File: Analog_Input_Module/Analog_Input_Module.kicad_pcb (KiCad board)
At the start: 2 copper layers, 60 x 22 mm, 63 parts, among them J1 Conn_02x20_Odd_Even, U1 10K, U10 1.5K, U11 MCP6004, U12 10K, U13 10K, U14 10nF, U15 10nF, U16 MCP6004, U17 1K, U18 1K, U19 1.5K, U2 10K, U20 1.5K, U3 10nF, U4 10nF, U5 MCP6004, U6 MCP6004, U7 1K, U8 1K, U9 1.5K

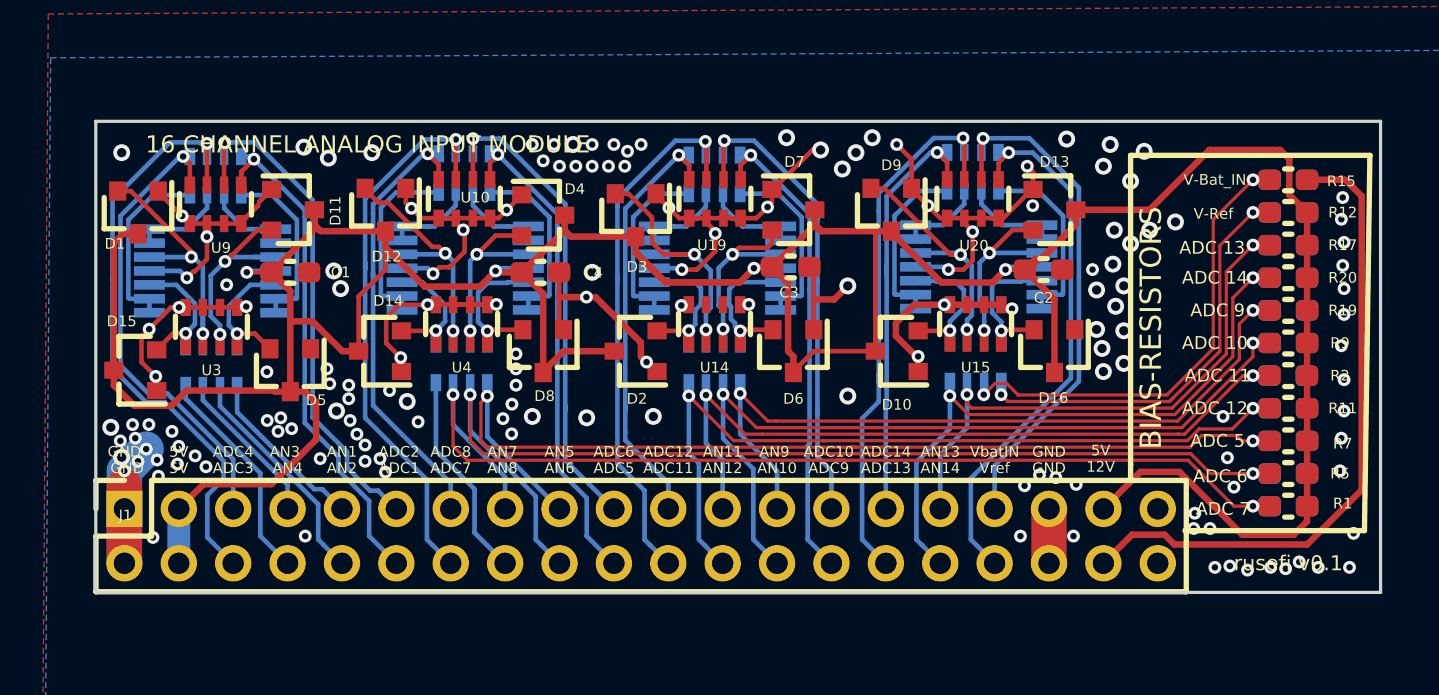
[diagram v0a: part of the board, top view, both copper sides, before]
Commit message: Corrected diode symbols and cleaned sym-lib-table
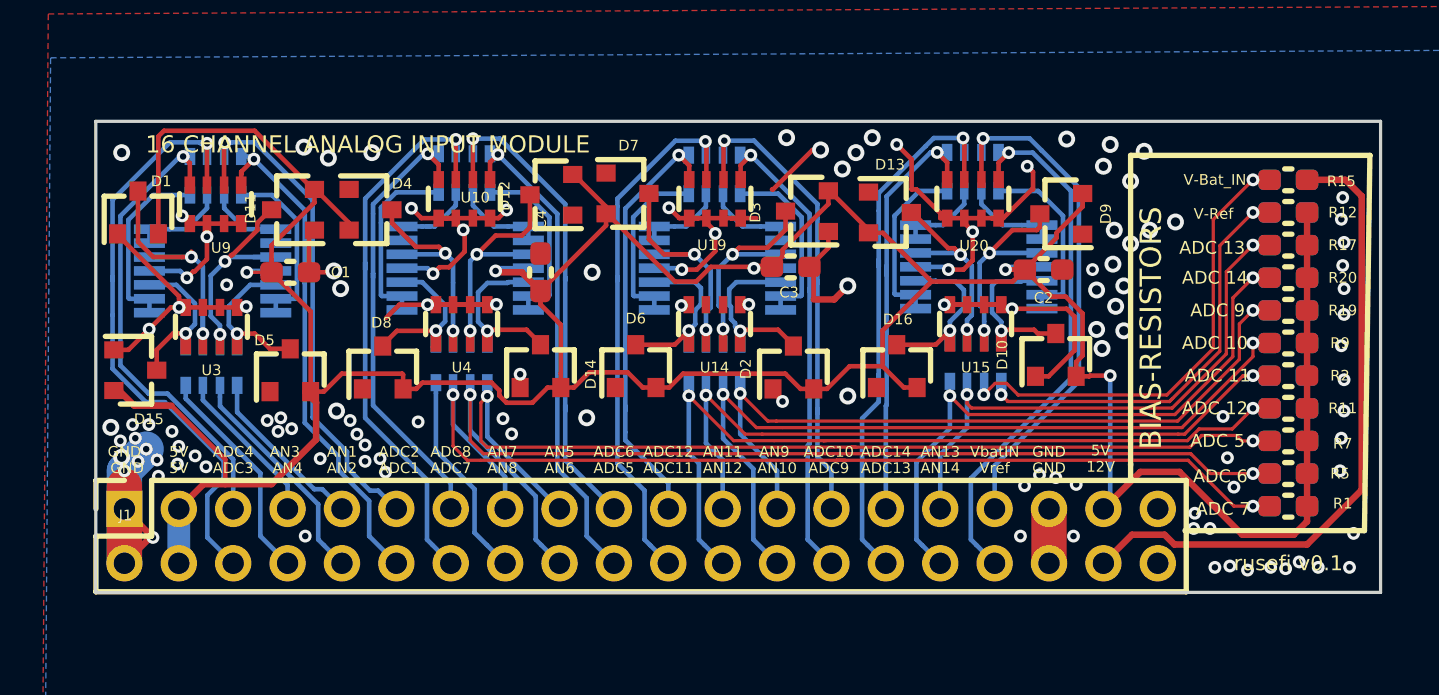
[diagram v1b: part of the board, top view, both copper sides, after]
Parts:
- moved D4 8.07 mm to (32.8, 24.1)
- moved D3 8.00 mm to (53.2, 24.2), turned to 180 degrees
- moved D9 7.94 mm to (65.1, 24.3), turned to 180 degrees
- moved D7 7.78 mm to (44.8, 23.4)
- moved D12 7.78 mm to (41.3, 23.4), turned to 180 degrees
- moved D13 7.68 mm to (57.1, 24.3)
- moved D8 7.53 mm to (33.4, 31.5), turned to 90 degrees
- moved D14 7.53 mm to (40.8, 31.4), turned to 90 degrees
- moved D10 7.43 mm to (64.8, 30.9), turned to 90 degrees
- moved D2 7.41 mm to (52.6, 31.5), turned to 90 degrees
- moved D6 7.40 mm to (45.2, 31.4), turned to 90 degrees
- moved D16 7.40 mm to (57.4, 31.4), turned to 90 degrees
- turned C4 to 90 degrees
- turned D1 to 90 degrees
- turned D11 to 180 degrees
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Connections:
- D1 pad 2: Net-(D1-Pad2) -> /5V
- D1 pad 3: /5V -> Net-(D1-Pad3)
- D10 pad 2: Net-(D10-Pad2) -> /5V
- D10 pad 3: /5V -> Net-(D10-Pad3)
- D11 pad 2: Net-(D11-Pad2) -> /5V
- D11 pad 3: /5V -> Net-(D11-Pad3)
- D12 pad 2: Net-(D12-Pad2) -> /5V
- D12 pad 3: /5V -> Net-(D12-Pad3)
- D13 pad 2: Net-(D13-Pad2) -> /5V
- D13 pad 3: /5V -> Net-(D13-Pad3)
- D14 pad 2: Net-(D14-Pad2) -> /5V
- D14 pad 3: /5V -> Net-(D14-Pad3)
- D15 pad 2: Net-(D15-Pad2) -> /5V
- D15 pad 3: /5V -> Net-(D15-Pad3)
- D16 pad 2: Net-(D16-Pad2) -> /5V
- D16 pad 3: /5V -> Net-(D16-Pad3)
- D2 pad 2: Net-(D2-Pad2) -> /5V
- D2 pad 3: /5V -> Net-(D2-Pad3)
- D3 pad 2: Net-(D3-Pad2) -> /5V
- D3 pad 3: /5V -> Net-(D3-Pad3)
- D4 pad 2: Net-(D4-Pad2) -> /5V
- D4 pad 3: /5V -> Net-(D4-Pad3)
- D5 pad 2: Net-(D5-Pad2) -> /5V
- D5 pad 3: /5V -> Net-(D5-Pad3)
- D6 pad 2: Net-(D6-Pad2) -> /5V
- D6 pad 3: /5V -> Net-(D6-Pad3)
- D7 pad 2: Net-(D7-Pad2) -> /5V
- D7 pad 3: /5V -> Net-(D7-Pad3)
- D8 pad 2: Net-(D8-Pad2) -> /5V
- D8 pad 3: /5V -> Net-(D8-Pad3)
- D9 pad 2: Net-(D9-Pad2) -> /5V
- D9 pad 3: /5V -> Net-(D9-Pad3)
- U1 pad 5: Net-(D15-Pad2) -> Net-(D15-Pad3)
- U1 pad 6: Net-(D1-Pad2) -> Net-(D1-Pad3)
- U1 pad 7: Net-(D11-Pad2) -> Net-(D11-Pad3)
- U1 pad 8: Net-(D5-Pad2) -> Net-(D5-Pad3)
- U11 pad 10: Net-(D2-Pad2) -> Net-(D6-Pad3)
- U11 pad 12: Net-(D3-Pad2) -> Net-(D7-Pad3)
- U11 pad 3: Net-(D7-Pad2) -> Net-(D3-Pad3)
- U11 pad 5: Net-(D6-Pad2) -> Net-(D2-Pad3)
- U12 pad 5: Net-(D2-Pad2) -> Net-(D6-Pad3)
- U12 pad 6: Net-(D3-Pad2) -> Net-(D7-Pad3)
- U12 pad 7: Net-(D7-Pad2) -> Net-(D3-Pad3)
- U12 pad 8: Net-(D6-Pad2) -> Net-(D2-Pad3)
- U13 pad 5: Net-(D10-Pad2) -> Net-(D16-Pad3)
- U13 pad 6: Net-(D9-Pad2) -> Net-(D13-Pad3)
- U13 pad 7: Net-(D13-Pad2) -> Net-(D9-Pad3)
- U13 pad 8: Net-(D16-Pad2) -> Net-(D10-Pad3)
- U14 pad 1: Net-(D2-Pad2) -> Net-(D6-Pad3)
- U14 pad 2: Net-(D3-Pad2) -> Net-(D7-Pad3)
- U14 pad 3: Net-(D7-Pad2) -> Net-(D3-Pad3)
- U14 pad 4: Net-(D6-Pad2) -> Net-(D2-Pad3)
- U15 pad 1: Net-(D10-Pad2) -> Net-(D16-Pad3)
- U15 pad 2: Net-(D9-Pad2) -> Net-(D13-Pad3)
- U15 pad 3: Net-(D13-Pad2) -> Net-(D9-Pad3)
- U15 pad 4: Net-(D16-Pad2) -> Net-(D10-Pad3)
- U16 pad 10: Net-(D10-Pad2) -> Net-(D16-Pad3)
- U16 pad 12: Net-(D9-Pad2) -> Net-(D13-Pad3)
- U16 pad 3: Net-(D13-Pad2) -> Net-(D9-Pad3)
- U16 pad 5: Net-(D16-Pad2) -> Net-(D10-Pad3)
- U2 pad 5: Net-(D14-Pad2) -> Net-(D8-Pad3)
- U2 pad 6: Net-(D12-Pad2) -> Net-(D4-Pad3)
- U2 pad 7: Net-(D4-Pad2) -> Net-(D12-Pad3)
- U2 pad 8: Net-(D8-Pad2) -> Net-(D14-Pad3)
- U3 pad 1: Net-(D15-Pad2) -> Net-(D15-Pad3)
- U3 pad 2: Net-(D1-Pad2) -> Net-(D1-Pad3)
- U3 pad 3: Net-(D11-Pad2) -> Net-(D11-Pad3)
- U3 pad 4: Net-(D5-Pad2) -> Net-(D5-Pad3)
- U4 pad 1: Net-(D14-Pad2) -> Net-(D8-Pad3)
- U4 pad 2: Net-(D12-Pad2) -> Net-(D4-Pad3)
- U4 pad 3: Net-(D4-Pad2) -> Net-(D12-Pad3)
- U4 pad 4: Net-(D8-Pad2) -> Net-(D14-Pad3)
- U5 pad 10: Net-(D15-Pad2) -> Net-(D15-Pad3)
- U5 pad 12: Net-(D1-Pad2) -> Net-(D1-Pad3)
- U5 pad 3: Net-(D11-Pad2) -> Net-(D11-Pad3)
- U5 pad 5: Net-(D5-Pad2) -> Net-(D5-Pad3)
- U6 pad 10: Net-(D14-Pad2) -> Net-(D8-Pad3)
- U6 pad 12: Net-(D12-Pad2) -> Net-(D4-Pad3)
- U6 pad 3: Net-(D4-Pad2) -> Net-(D12-Pad3)
- U6 pad 5: Net-(D8-Pad2) -> Net-(D14-Pad3)
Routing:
- net Net-(D1-Pad3): track 0.00 -> 16.1 mm, vias 0 -> 2
- net Net-(D1-Pad2): track 15.6 -> 0.00 mm, vias 2 -> 0
- net Net-(D9-Pad2): track 13.6 -> 0.00 mm, vias 2 -> 0
- net GND: track 118.2 -> 104.8 mm, vias 157 -> 123
- net Net-(D3-Pad2): track 12.7 -> 0.00 mm, vias 2 -> 0
- net Net-(D12-Pad2): track 12.0 -> 0.00 mm, vias 2 -> 0
- net Net-(D11-Pad3): track 0.00 -> 11.9 mm, vias 0 -> 2
- net Net-(D12-Pad3): track 0.00 -> 11.8 mm, vias 0 -> 2
- net Net-(D7-Pad3): track 0.00 -> 11.7 mm, vias 0 -> 2
- net /5V: track 191.2 -> 179.8 mm, vias 4 -> 5
- net Net-(D11-Pad2): track 11.3 -> 0.00 mm, vias 2 -> 0
- net Net-(D3-Pad3): track 0.00 -> 11.3 mm, vias 0 -> 2
- net Net-(D13-Pad3): track 0.00 -> 11.3 mm, vias 0 -> 2
- net Net-(D9-Pad3): track 0.00 -> 11.0 mm, vias 0 -> 2
- net Net-(D4-Pad3): track 0.00 -> 10.7 mm, vias 0 -> 2
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
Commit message: manual sync
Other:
- board text added: "rusefi v0.2"
- board text removed: "rusefi v0.1"

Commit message: V 0.3 (#30)
* gerbers

* version

* V 0.3
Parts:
- removed U1, U12, U13, U2: 10K, Resistor_SMD:R_Array_Convex_4x0603
- removed U10, U19, U20, U9: 1.5K, Resistor_SMD:R_Array_Convex_4x0603
- removed U14, U15, U3, U4: 10nF, Resistor_SMD:R_Array_Convex_4x0603
- removed U17, U18, U7, U8: 1K, Resistor_SMD:R_Array_Convex_4x0603
- added C10: 10nF, Capacitor_SMD:C_0402_1005Metric, B.Cu at (49.3, 29.1)
- added C11: 10nF, Capacitor_SMD:C_0402_1005Metric, B.Cu at (38.6, 24.7)
- added C12: 10nF, Capacitor_SMD:C_0402_1005Metric, B.Cu at (41.1, 33.8)
- added C13: 10nF, Capacitor_SMD:C_0402_1005Metric, B.Cu at (77.8, 33.4)
- added C14: 10nF, Capacitor_SMD:C_0402_1005Metric, B.Cu at (61.9, 33.6)
- added C15: 10nF, Capacitor_SMD:C_0402_1005Metric, B.Cu at (75.8, 22.4)
- added C16: 10nF, Capacitor_SMD:C_0402_1005Metric, B.Cu at (63.6, 27.8)
- added C17: 10nF, Capacitor_SMD:C_0402_1005Metric, B.Cu at (69.0, 24.7)
- added C18: 10nF, Capacitor_SMD:C_0402_1005Metric, B.Cu at (53.4, 26.0)
- added C19: 10nF, Capacitor_SMD:C_0402_1005Metric, B.Cu at (71.6, 33.4)
- added C20: 10nF, Capacitor_SMD:C_0402_1005Metric, B.Cu at (55.4, 33.4)
- added C5: 10nF, Capacitor_SMD:C_0402_1005Metric, B.Cu at (32.8, 33.9)
- added C6: 10nF, Capacitor_SMD:C_0402_1005Metric, B.Cu at (34.8, 24.7)
- added C7: 10nF, Capacitor_SMD:C_0402_1005Metric, B.Cu at (23.5, 26.7)
- added C8: 10nF, Capacitor_SMD:C_0402_1005Metric, B.Cu at (26.4, 33.8)
- added C9: 10nF, Capacitor_SMD:C_0402_1005Metric, B.Cu at (47.6, 33.8)
- added R23: 1.5K, Capacitor_SMD:C_0402_1005Metric, B.Cu at (62.3, 22.6)
- added R24: 1.5K, Capacitor_SMD:C_0402_1005Metric, B.Cu at (60.3, 22.6)
- added R25: 1.5K, Capacitor_SMD:C_0402_1005Metric, B.Cu at (57.2, 22.6)
- added R26: 1.5K, Capacitor_SMD:C_0402_1005Metric, B.Cu at (55.2, 22.6)
- added R27: 1K, Capacitor_SMD:C_0402_1005Metric, B.Cu at (61.3, 22.3)
- added R28: 1K, Capacitor_SMD:C_0402_1005Metric, B.Cu at (59.3, 22.6)
- added R29: 1K, Capacitor_SMD:C_0402_1005Metric, B.Cu at (58.2, 22.6)
- added R30: 1K, Capacitor_SMD:C_0402_1005Metric, B.Cu at (56.2, 22.3)
- added R31: 10K, Capacitor_SMD:C_0402_1005Metric, B.Cu at (45.7, 31.0)
- added R32: 10K, Capacitor_SMD:C_0402_1005Metric, B.Cu at (44.7, 31.0)
- added R33: 10K, Capacitor_SMD:C_0402_1005Metric, B.Cu at (43.7, 31.0)
- added R34: 10K, Capacitor_SMD:C_0402_1005Metric, B.Cu at (42.7, 31.0)
- added R35: 10K, Capacitor_SMD:C_0402_1005Metric, B.Cu at (60.3, 30.7)
- added R36: 10K, Capacitor_SMD:C_0402_1005Metric, B.Cu at (59.3, 30.7)
- added R37: 10K, Capacitor_SMD:C_0402_1005Metric, B.Cu at (58.2, 30.7)
- added R38: 10K, Capacitor_SMD:C_0402_1005Metric, B.Cu at (57.2, 30.7)
- added R39: 10K, Capacitor_SMD:C_0402_1005Metric, B.Cu at (30.7, 31.2)
- added R40: 10K, Capacitor_SMD:C_0402_1005Metric, B.Cu at (29.7, 31.2)
- added R41: 10K, Capacitor_SMD:C_0402_1005Metric, B.Cu at (28.7, 31.2)
- added R42: 10K, Capacitor_SMD:C_0402_1005Metric, B.Cu at (27.7, 31.2)
- added R43: 1.5K, Capacitor_SMD:C_0402_1005Metric, B.Cu at (32.4, 23.1)
- added R44: 1.5K, Capacitor_SMD:C_0402_1005Metric, B.Cu at (30.4, 23.0)
- added R45: 1.5K, Capacitor_SMD:C_0402_1005Metric, B.Cu at (27.3, 23.0)
- added R46: 1.5K, Capacitor_SMD:C_0402_1005Metric, B.Cu at (25.3, 23.1)
- added R47: 1K, Capacitor_SMD:C_0402_1005Metric, B.Cu at (31.4, 22.7)
- added R48: 1K, Capacitor_SMD:C_0402_1005Metric, B.Cu at (29.3, 23.0)
- added R49: 1K, Capacitor_SMD:C_0402_1005Metric, B.Cu at (28.3, 23.0)
- added R50: 1K, Capacitor_SMD:C_0402_1005Metric, B.Cu at (26.3, 22.6)
- added R51: 1.5K, Capacitor_SMD:C_0402_1005Metric, B.Cu at (48.1, 23.0)
- added R52: 1.5K, Capacitor_SMD:C_0402_1005Metric, B.Cu at (46.1, 22.9)
- added R53: 1.5K, Capacitor_SMD:C_0402_1005Metric, B.Cu at (43.1, 23.0)
- added R54: 1.5K, Capacitor_SMD:C_0402_1005Metric, B.Cu at (41.0, 23.0)
- added R55: 1K, Capacitor_SMD:C_0402_1005Metric, B.Cu at (47.1, 22.5)
- added R56: 1K, Capacitor_SMD:C_0402_1005Metric, B.Cu at (45.1, 23.0)
- added R57: 1K, Capacitor_SMD:C_0402_1005Metric, B.Cu at (44.1, 23.0)
- added R58: 1K, Capacitor_SMD:C_0402_1005Metric, B.Cu at (42.0, 22.6)
- added R59: 10K, Capacitor_SMD:C_0402_1005Metric, B.Cu at (76.3, 30.6)
- added R60: 10K, Capacitor_SMD:C_0402_1005Metric, B.Cu at (75.3, 30.6)
- added R61: 10K, Capacitor_SMD:C_0402_1005Metric, B.Cu at (74.2, 30.6)
- added R62: 10K, Capacitor_SMD:C_0402_1005Metric, B.Cu at (73.2, 30.6)
- added R63: 1.5K, Capacitor_SMD:C_0402_1005Metric, B.Cu at (77.8, 22.3)
- added R64: 1.5K, Capacitor_SMD:C_0402_1005Metric, B.Cu at (77.5, 37.0)
- added R65: 1.5K, Capacitor_SMD:C_0402_1005Metric, B.Cu at (73.4, 22.4)
- added R66: 1.5K, Capacitor_SMD:C_0402_1005Metric, B.Cu at (71.3, 22.4)
- added R67: 1K, Capacitor_SMD:C_0402_1005Metric, B.Cu at (78.9, 22.3)
- added R68: 1K, Capacitor_SMD:C_0402_1005Metric, B.Cu at (78.5, 37.0)
- added R69: 1K, Capacitor_SMD:C_0402_1005Metric, B.Cu at (74.4, 22.4)
- added R70: 1K, Capacitor_SMD:C_0402_1005Metric, B.Cu at (72.3, 22.2)
- C1, C2, C3, C4: value 0.1uF -> 100nF; footprint Capacitor_SMD:C_0603_1608Metric_Pad1.05x0.95mm_HandSolder -> Capacitor_SMD:C_0402_1005Metric; moved to B.Cu
- D1, D10, D11, D12, D13, D14, D15, D16, D2, D3, D4, D5, D6, D7, D8, D9, R1, R11, R12, R15, R17, R19, R2, R20, R5, R7, R9: moved to B.Cu
- moved R10 19.4 mm to (95.1, 29.2)
- moved R13 19.4 mm to (95.1, 32.2)
- moved R14 19.4 mm to (95.1, 23.1)
- moved R16 19.4 mm to (95.1, 21.5)
- moved R18 19.4 mm to (95.1, 24.6)
- moved R21 19.4 mm to (95.1, 27.6)
- moved R22 19.4 mm to (95.1, 26.1)
- moved R3 19.4 mm to (95.1, 36.8)
- moved R4 19.4 mm to (95.1, 30.7)
- moved R6 19.4 mm to (95.1, 35.3)
- moved R8 19.4 mm to (95.1, 33.7)
- moved C2 16.3 mm to (80.6, 27.0), turned to 270 degrees
- moved R1 15.2 mm to (90.9, 36.8), turned to 180 degrees
- moved R11 15.2 mm to (90.9, 32.2), turned to 180 degrees
- moved R12 15.2 mm to (90.9, 23.1), turned to 180 degrees
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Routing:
- net /5V: track 179.8 -> 239.6 mm, vias 5 -> 22
- net /U-Batt: track 30.4 -> 54.5 mm, vias 0 -> 1
- net Net-(R64-Pad2): track 4.50 -> 26.0 mm
- net /ADC_14: track 29.9 -> 47.4 mm
- net /ADC_12: track 38.6 -> 55.0 mm
- net /ADC_13: track 27.3 -> 43.6 mm
- net /ADC_10: track 38.4 -> 52.6 mm
- net /ADC_11: track 36.4 -> 50.5 mm
- net /ADC_9: track 35.7 -> 48.9 mm
- net /ADC_7: track 49.8 -> 62.4 mm
- net /ADC_6: track 51.1 -> 63.7 mm
- net /ADC_5: track 47.9 -> 60.2 mm
- net /U-Batt_MCU: track 24.8 -> 14.7 mm, vias 1 -> 0
- net /Vref: track 25.4 -> 35.4 mm, vias 1 -> 0
- net Net-(C15-Pad1): track 11.0 -> 19.4 mm
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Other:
- board size 60 x 22 mm -> 81 x 22 mm
- board text added: "rusefi v0.3"
- board text removed: "rusefi v0.2"
